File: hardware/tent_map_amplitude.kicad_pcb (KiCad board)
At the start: 4 copper layers, 56.4 x 58.4 mm, 50 parts, among them U1 LM339AN, U2 TL082IP, U3 TL082IP, U4 LF398_DIP8, U5 LF398_DIP8, U6 LF398_DIP8

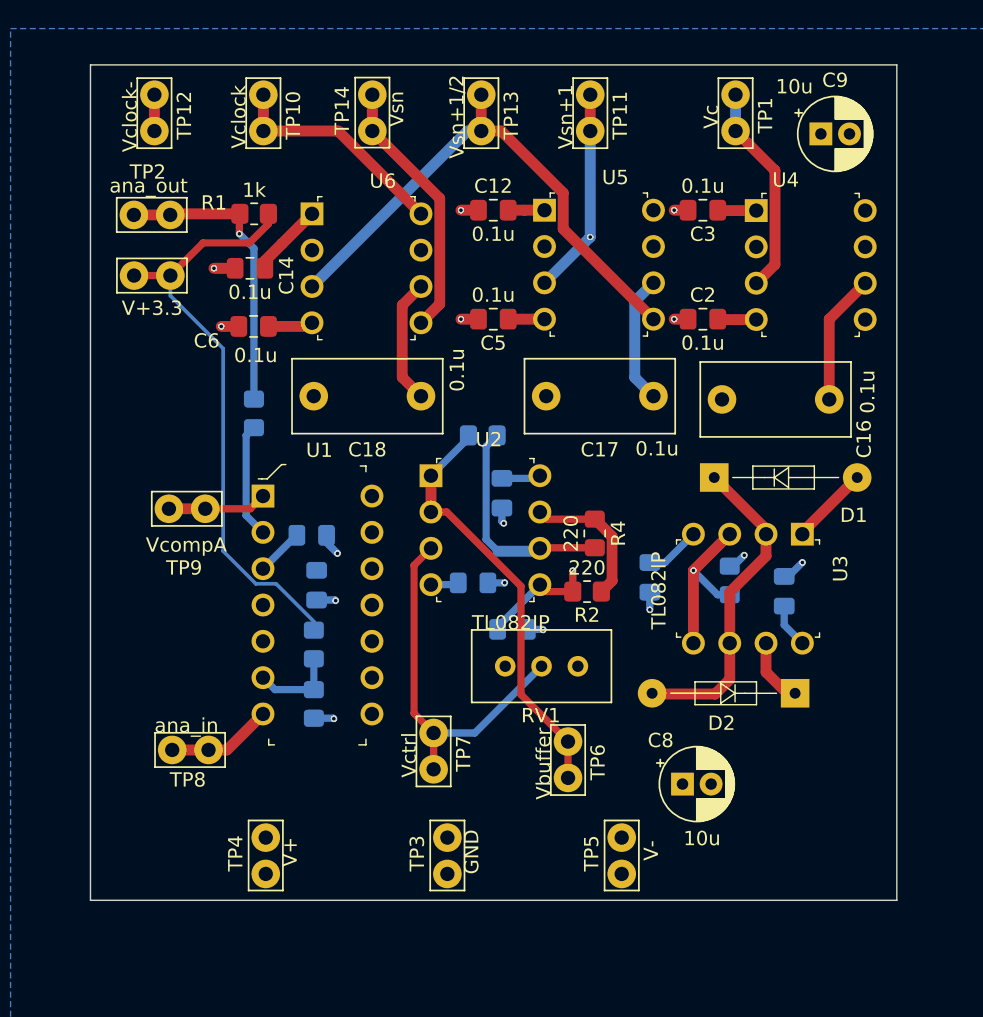
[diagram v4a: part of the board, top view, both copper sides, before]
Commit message: Go back to old board design with all components on front, Merge previous changes
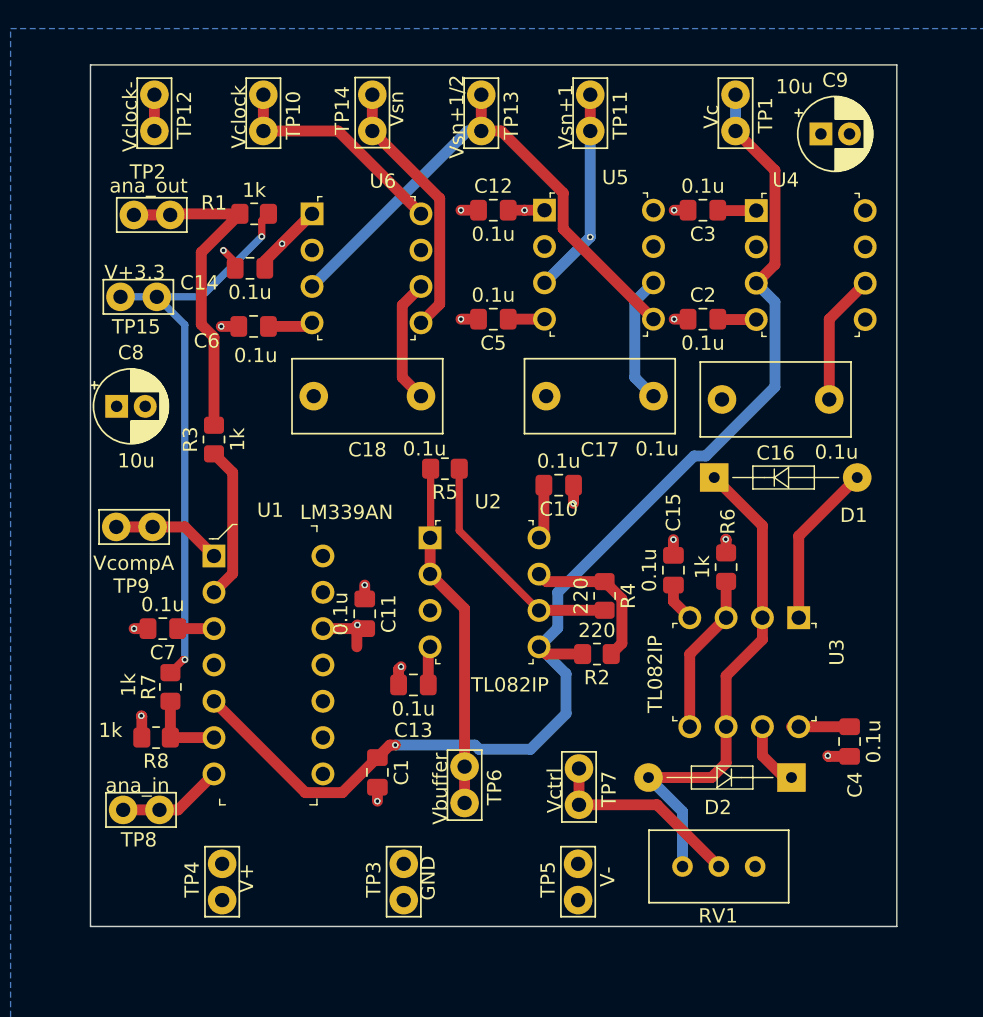
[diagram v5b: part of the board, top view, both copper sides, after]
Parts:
- C1, C10, C11, C13, C15, C4, C7, R3, R5, R6, R7, R8: moved to F.Cu
- moved C8 47.6 mm to (68.4, 77.2)
- moved RV1 18.7 mm to (108.0, 109.4)
- moved C1 13.8 mm to (86.6, 102.8), turned to 270 degrees
- moved C7 12.3 mm to (71.6, 92.8), turned to 180 degrees
- moved C4 11.5 mm to (119.6, 100.7), turned to 90 degrees
- moved R8 11.3 mm to (71.1, 100.4), turned to 180 degrees
- moved TP7 10.5 mm to (100.7, 105.1)
- moved R7 10.5 mm to (72.1, 96.8)
- moved C13 8.26 mm to (89.1, 96.7), turned to 0 degrees
- moved TP6 7.44 mm to (92.7, 105.0)
- moved D2 5.90 mm to (115.6, 103.2)
- moved U3 5.85 mm to (116.1, 92.0)
- moved TP8 5.42 mm to (68.8, 105.4)
- moved U1 5.42 mm to (75.2, 87.7)
- moved R4 4.42 mm to (102.5, 90.5)
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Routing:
- net Net-(C1-Pad1): track 70.6 -> 86.7 mm
- net Net-(R6-Pad2): track 51.7 -> 61.9 mm, vias 1 -> 0
- net Net-(D1-Pad2): track 5.78 -> 11.5 mm
- net Net-(R5-Pad2): track 29.7 -> 24.4 mm
- net V-: track 14.4 -> 18.3 mm, vias 0 -> 1
- net Net-(RV1-Pad2): track 26.0 -> 29.5 mm
- net Net-(R1-Pad2): track 20.8 -> 23.7 mm, vias 1 -> 0
- net Net-(R3-Pad1): track 8.04 -> 10.8 mm
- net Net-(D1-Pad1): track 32.9 -> 35.5 mm
- net Net-(R4-Pad2): track 15.6 -> 16.8 mm
- net V+: track 25.6 -> 26.5 mm, vias 1 -> 3
- net GND: track 17.9 -> 17.0 mm
- net Net-(R2-Pad1): track 9.92 -> 10.7 mm
- net +3V3: track 41.4 -> 41.0 mm, vias 0 -> 2
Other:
- board size 56.4 x 58.4 mm -> 56.4 x 60.2 mm

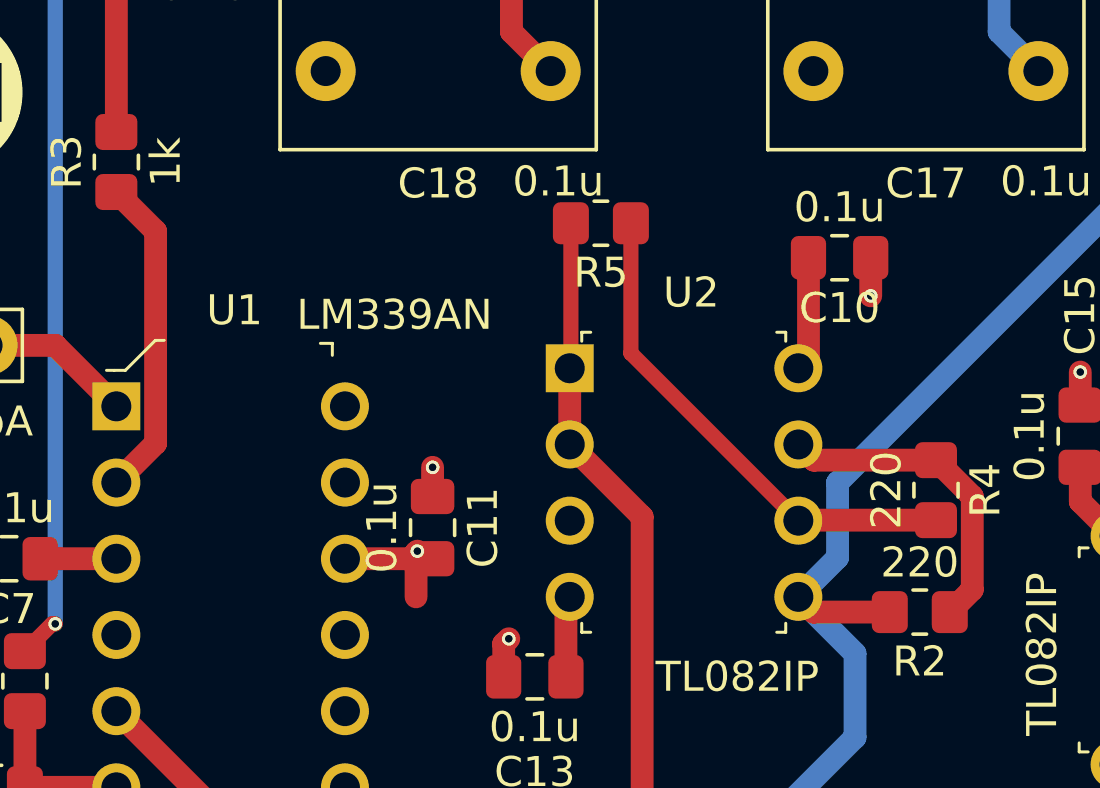
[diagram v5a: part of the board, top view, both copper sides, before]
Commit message: Remove some uneeded traces and vias
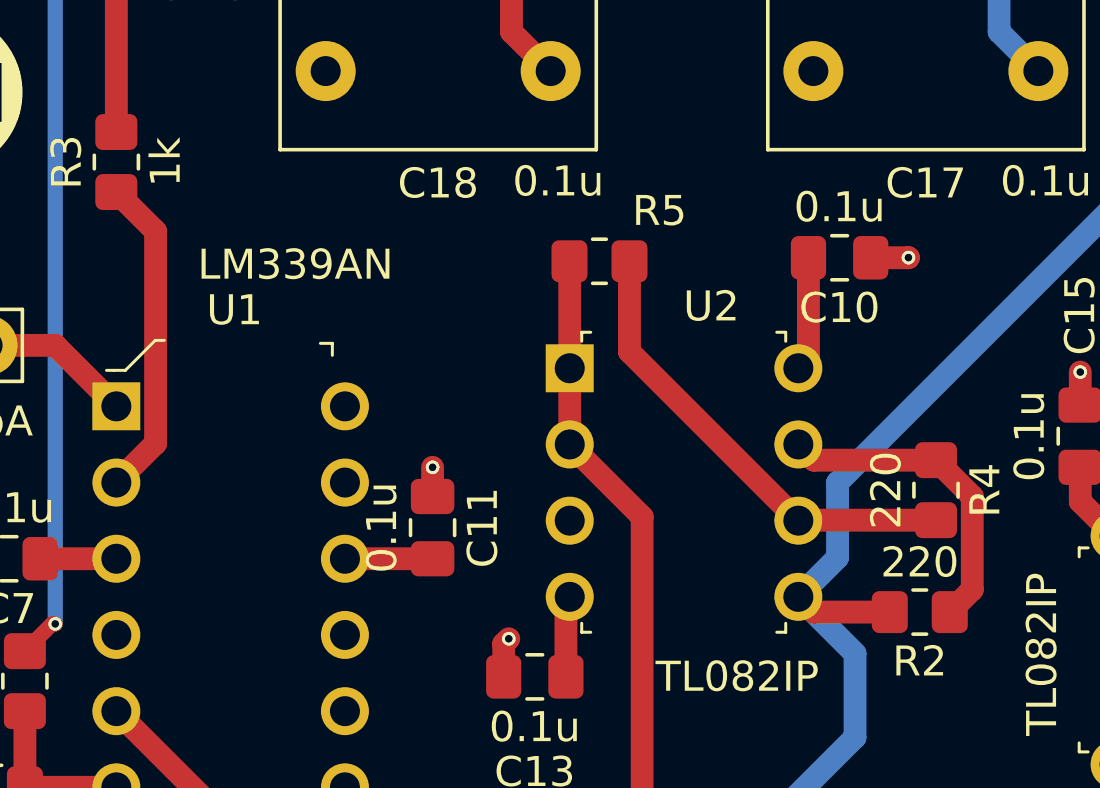
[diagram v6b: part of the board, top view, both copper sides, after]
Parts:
- moved R5 1.27 mm to (91.3, 82.8)
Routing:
- net V-: track 18.3 -> 16.8 mm, vias 1 -> 0
- net Net-(R5-Pad2): track 24.4 -> 23.1 mm
- net Net-(R4-Pad2): track 16.8 -> 15.6 mm
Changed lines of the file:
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@@
     (thickness 1.6002)
     (drawings 5)
-    (tracks 203)
+    (tracks 201)
     (zones 0)
     (modules 50)
@@
   )
   (module Resistor_SMD:R_0805_2012Metric_Pad1.20x1.40mm_HandSolder (layer Front)
-    (at 91.3351 81.57718 180)
+    (at 91.2876 82.84464 180)
     (descr "Resistor SMD 0805 (2012 Metric), square (rectangular) end terminal, IPC_7351 nominal with elongated pad for handsoldering. (Body size source: IPC-SM-782 page 72, https://www.pcb-3d.com/wordpress/wp-content/uploads/ipc-sm-782a_amendment_1_and_2.pdf), generated with kicad-footprint-generator")
     (tags "resistor handsolder")
     (attr smd)
-    (fp_text reference R5 (at 0 -1.65) (layer F.SilkS)
+    (fp_text reference R5 (at -2.00152 1.67386) (layer F.SilkS)
       (effects (font (size 1 1) (thickness 0.15)))
     )
@@
     (at 90.297 86.4108)
     (descr http://media.digikey.com/pdf/Data%20Sheets/Lite-On%20PDFs/6N137%20Series.pdf)
-    (fp_text reference U2 (at 4.05 -2.52) (layer F.SilkS)
+    (fp_text reference U2 (at 4.72186 -2.0574) (layer F.SilkS)
       (effects (font (size 1 1) (thickness 0.15)))
     )
@@
       (effects (font (size 1 1) (thickness 0.15)))
     )
-    (fp_text value LM339AN (at 9.271 -3.048) (layer F.SilkS)
+    (fp_text value LM339AN (at 5.97154 -4.71932) (layer F.SilkS)
       (effects (font (size 1 1) (thickness 0.15)))
     )
@@
   (segment (start 88.095 95.5978) (end 88.265 95.4278) (width 0.762) (layer Front) (net 1))
   (segment (start 88.095 96.6978) (end 88.095 95.5978) (width 0.762) (layer Front) (net 1))
-  (segment (start 100.33 82.7278) (end 100.33 83.9978) (width 0.762) (layer Front) (net 1))
-  (via (at 100.33 83.9978) (size 0.4572) (drill 0.254) (layers Front Back) (net 1))
   (segment (start 76.665 67.13238) (end 75.84694 66.31432) (width 0.508) (layer Front) (net 1))
   (via (at 75.84694 66.31432) (size 0.4572) (drill 0.254) (layers Front Back) (net 1))
   (segment (start 76.665 67.564) (end 76.665 67.13238) (width 0.508) (layer Front) (net 1))
+  (via (at 101.5873 82.72272) (size 0.4572) (drill 0.254) (layers Front Back) (net 1))
+  (segment (start 101.58222 82.7278) (end 101.5873 82.72272) (width 0.762) (layer Front) (net 1))
+  (segment (start 100.33 82.7278) (end 101.58222 82.7278) (width 0.762) (layer Front) (net 1))
   (segment (start 98.425 94.5388) (end 97.917 94.0308) (width 0.762) (layer Front) (net 2))
   (segment (start 100.965 94.5388) (end 98.425 94.5388) (width 0.762) (layer Front) (net 2))
@@
   (segment (start 114.414201 69.913401) (end 114.414201 75.857199) (width 0.762) (layer Back) (net 2))
   (segment (start 113.1062 68.6054) (end 114.414201 69.913401) (width 0.762) (layer Back) (net 2))
-  (via (at 85.217 92.5068) (size 0.4572) (drill 0.254) (layers Front Back) (net 3))
-  (segment (start 85.174 92.5498) (end 85.217 92.5068) (width 0.762) (layer Front) (net 3))
-  (segment (start 85.174 94.0308) (end 85.174 92.5498) (width 0.762) (layer Front) (net 3))
   (segment (start 95.758 71.12) (end 98.298 71.12) (width 0.762) (layer Front) (net 3))
   (segment (start 81.788 71.628) (end 82.042 71.374) (width 0.762) (layer Front) (net 3))
@@
   (segment (start 97.933 91.4748) (end 97.917 91.4908) (width 0.762) (layer Front) (net 10))
   (segment (start 102.505 91.4748) (end 97.933 91.4748) (width 0.762) (layer Front) (net 10))
-  (segment (start 92.3351 85.9089) (end 97.917 91.4908) (width 0.508) (layer Front) (net 10))
-  (segment (start 92.3351 81.57718) (end 92.3351 85.9089) (width 0.508) (layer Front) (net 10))
+  (segment (start 92.2876 85.8614) (end 97.917 91.4908) (width 0.762) (layer Front) (net 10))
+  (segment (start 92.2876 82.84464) (end 92.2876 85.8614) (width 0.762) (layer Front) (net 10))
   (segment (start 90.297 86.4108) (end 90.297 88.9508) (width 0.762) (layer Front) (net 28))
   (segment (start 92.71 104.9528) (end 92.71 102.4128) (width 0.762) (layer Front) (net 28))
@@
   (segment (start 78.52664 64.22136) (end 78.994 63.754) (width 0.508) (layer Front) (net 27))
   (segment (start 78.52664 65.3415) (end 78.52664 64.22136) (width 0.508) (layer Front) (net 27))
-  (segment (start 90.3351 86.3727) (end 90.297 86.4108) (width 0.508) (layer Front) (net 28))
-  (segment (start 90.3351 81.57718) (end 90.3351 86.3727) (width 0.508) (layer Front) (net 28))
+  (segment (start 90.297 82.85404) (end 90.2876 82.84464) (width 0.762) (layer Front) (net 28))
+  (segment (start 90.297 86.4108) (end 90.297 82.85404) (width 0.762) (layer Front) (net 28))
   (zone (net 3) (net_name V-) (layer Back) (hatch edge 0.508)
     (connect_pads (clearance 0.508))
